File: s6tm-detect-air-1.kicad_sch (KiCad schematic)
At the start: 0 parts

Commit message: schem: import stm32f104 mcu
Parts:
- added C12: 10u, Capacitor_SMD:C_0805_2012Metric, symbol Device:C
- added C13, C16, C17, C18, C19: 0u1, Capacitor_SMD:C_0402_1005Metric, symbol Device:C
- added C14, C15: 20p, Capacitor_SMD:C_0603_1608Metric, symbol Device:C
- added C20, C21: 1u, Capacitor_SMD:C_0402_1005Metric, symbol Device:C
- added D10: YELLOW, LED_SMD:LED_0805_2012Metric, symbol Device:LED
- added D5, D6, D7, D8, D9: H5VU10U, GLCS:Diode_DFN1006, symbol GLCS:H5VU10U
- added FB1: 600Ω@100M, Inductor_SMD:L_0805_2012Metric, symbol Device:FerriteBead
- added J4: TC2030, Connector:Tag-Connect_TC2030-IDC-NL_2x03_P1.27mm_Vertical, symbol Connector:Conn_ARM_SWD_TagConnect_TC2030-NL
- added J5: Conn_01x04_Pin, Connector_PinHeader_2.54mm:PinHeader_1x04_P2.54mm_Vertical, symbol Connector:Conn_01x04_Pin
- added R10, R11, R9: 10k, Resistor_SMD:R_0402_1005Metric, symbol Device:R
- added R12: 560, Resistor_SMD:R_0603_1608Metric, symbol Device:R_Small
- added R13: 5k1, Resistor_SMD:R_0402_1005Metric, symbol Device:R
- added U6: STM32F103C8Tx, Package_QFP:LQFP-48_7x7mm_P0.5mm, symbol MCU_ST_STM32F1:STM32F103C8Tx
- added Y1: 8M, Crystal:Crystal_SMD_5032-2Pin_5.0x3.2mm, symbol Device:Crystal
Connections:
- new net: R13.1, U6.25 (PB12)
- new net: D10.2 (A), R13.2
- new net: C20.1, FB1.1, U6.9 (VDDA)
- new net +3V3: C12.1, C16.1, C17.1, C18.1, C19.1, C21.1, D9.1 (K), FB1.2, J4.1 (VCC), J5.1 (Pin_1), R10.1, R11.1, U6.1 (VBAT), U6.24 (VDD), U6.36 (VDD), U6.48 (VDD)
- new net BOOT: R9.2, U6.44 (BOOT0)
- new net CAN_RX: U6.45 (PB8)
- new net CAN_TX: U6.46 (PB9)
- new net GND: C12.2, C13.2, C14.2, C15.2, C16.2, C17.2, C18.2, C19.2, C20.2, C21.2, D10.1 (K), D5.2 (A), D6.2 (A), D7.2 (A), D8.2 (A), D9.2 (A), J4.5 (GND), J5.3 (Pin_3), R9.1, U6.20 (PB2), U6.23 (VSS), U6.35 (VSS), U6.47 (VSS), U6.8 (VSSA)
- new net NRST: C13.1, D8.1 (K), J4.3 (~{RESET}), U6.7 (NRST)
- new net SCL: R11.2
- new net SDA: R10.2
- new net SWCLK: D7.1 (K), J4.4 (SWCLK), U6.37 (PA14)
- new net SWDIO: D6.1 (K), J4.2 (SWDIO), U6.34 (PA13)
- new net SWO: D5.1 (K), J4.6 (SWO), U6.39 (PB3)
- new net U0RXD: J5.2 (Pin_2), U6.13 (PA3)
- new net U0TXD: J5.4 (Pin_4), U6.12 (PA2)
- new net XTAL_I: C14.1, U6.5 (PD0), Y1.2
- new net XTAL_O: R12.2, U6.6 (PD1)
- new net XTAL_RO: C15.1, R12.1, Y1.1
- no-connect marks 0 -> 5
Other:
- note added: "CAN Alive"
- note added: "Debug port"
- note added: "HSE"
- note added: "UART"

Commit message: schem: import HT753-1 3V3 LDO
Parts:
- added C1, C4: 10u, Capacitor_SMD:C_0805_2012Metric, symbol Device:C
- added TP2: TestPoint, TestPoint:TestPoint_Pad_D2.0mm, symbol Connector:TestPoint
- added U1: HT753-1, Package_TO_SOT_SMD:SOT-89-3, symbol Regulator_Linear:HT75xx-1-SOT89
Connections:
- net +3V3: now also C4.1, TP2.1, U1.3 (VOUT)
- net GND: now also C1.2, C4.2, U1.1 (GND)
- new net +5V: C1.1, U1.2 (VIN)
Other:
- note added: "HT753-1 3V3 LDO"

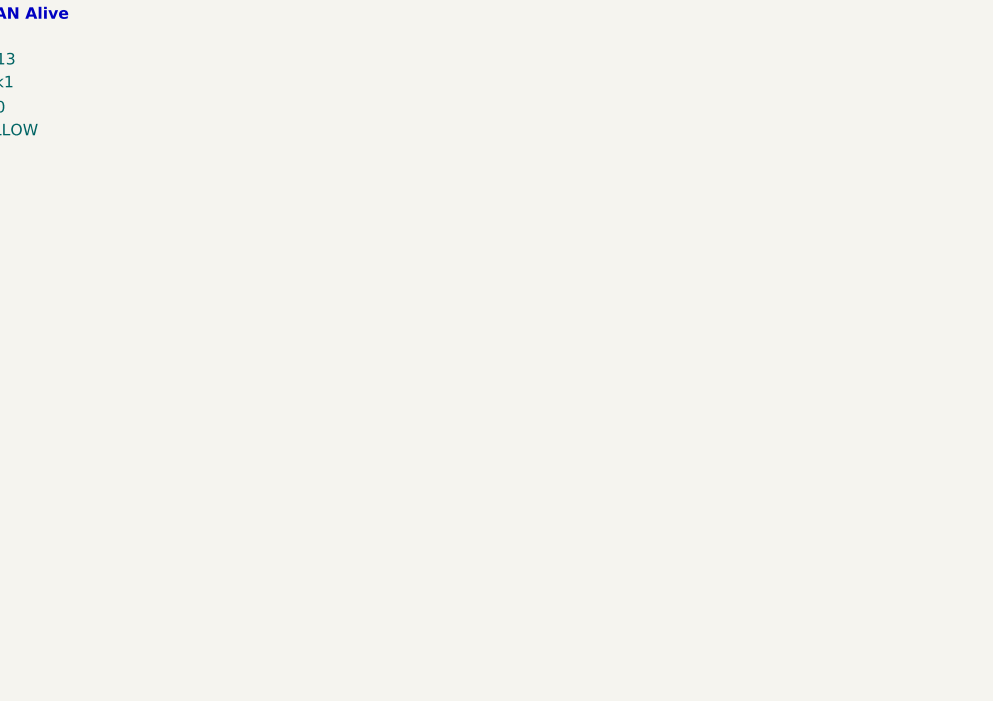
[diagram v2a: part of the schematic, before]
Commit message: schem: add LM73100 5V Input protection
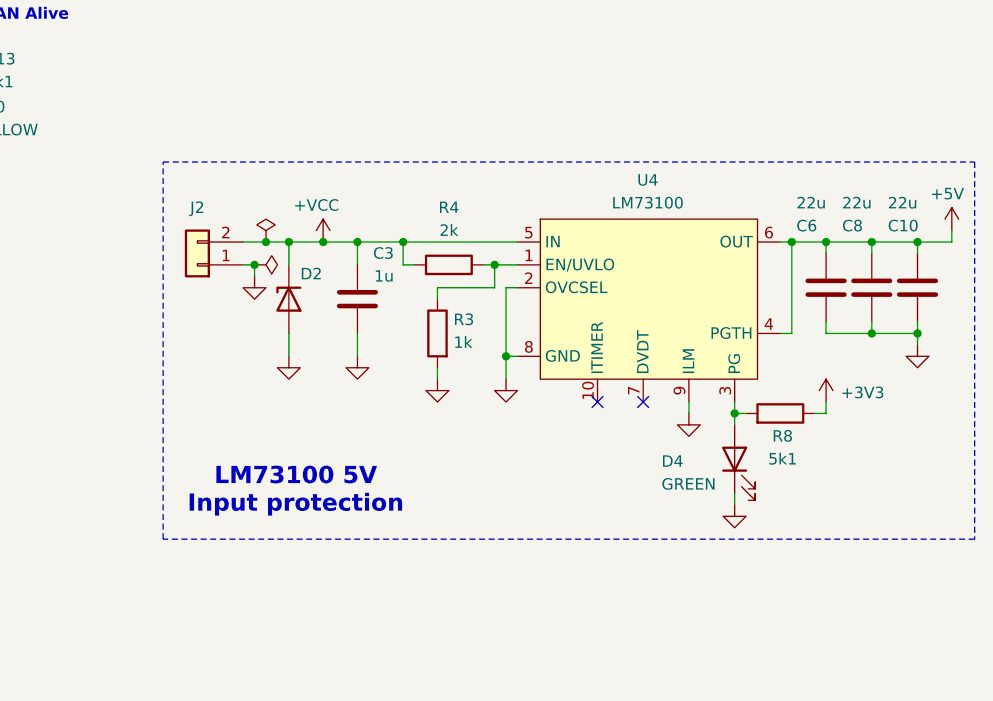
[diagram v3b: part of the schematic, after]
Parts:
- added C10, C6, C8: 22u, Capacitor_SMD:C_0805_2012Metric, symbol Device:C
- added C3: 1u, Capacitor_SMD:C_0402_1005Metric, symbol Device:C
- added D2: SMAJ12A, Diode_SMD:D_SMA, symbol Pers:H5VU10U
- added D4: GREEN, LED_SMD:LED_0805_2012Metric, symbol Device:LED
- added J2: Conn_01x02, TerminalBlock_Phoenix:TerminalBlock_Phoenix_MKDS-1,5-2-5.08_1x02_P5.08mm_Horizontal, symbol Connector_Generic:Conn_01x02
- added R3: 1k, Resistor_SMD:R_0402_1005Metric, symbol Device:R
- added R4: 2k, Resistor_SMD:R_0402_1005Metric, symbol Device:R
- added R8: 5k1, Resistor_SMD:R_0402_1005Metric, symbol Device:R
- added U4: LM73100, GLCS:Texas_RPW0010A_VQFN-HR-10_2x2mm_P0.5mm, symbol GLCS:LM73100
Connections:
- net +3V3: now also R8.1
- net +5V: now also C10.2, C6.2, C8.2, U4.4 (PGTH), U4.6 (OUT)
- net GND: now also C10.1, C3.1, C6.1, C8.1, D2.2 (A), D4.1 (K), J2.1 (Pin_1), R3.2, U4.2 (OVCSEL), U4.8 (GND), U4.9 (ILM)
- new net: D4.2 (A), R8.2, U4.3 (PG)
- new net: R3.1, R4.1, U4.1 (EN/UVLO)
- new net +VCC: C3.2, D2.1 (K), J2.2 (Pin_2), R4.2, U4.5 (IN)
- no-connect marks 5 -> 7
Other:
- note added: "LM73100 5V Input protection"

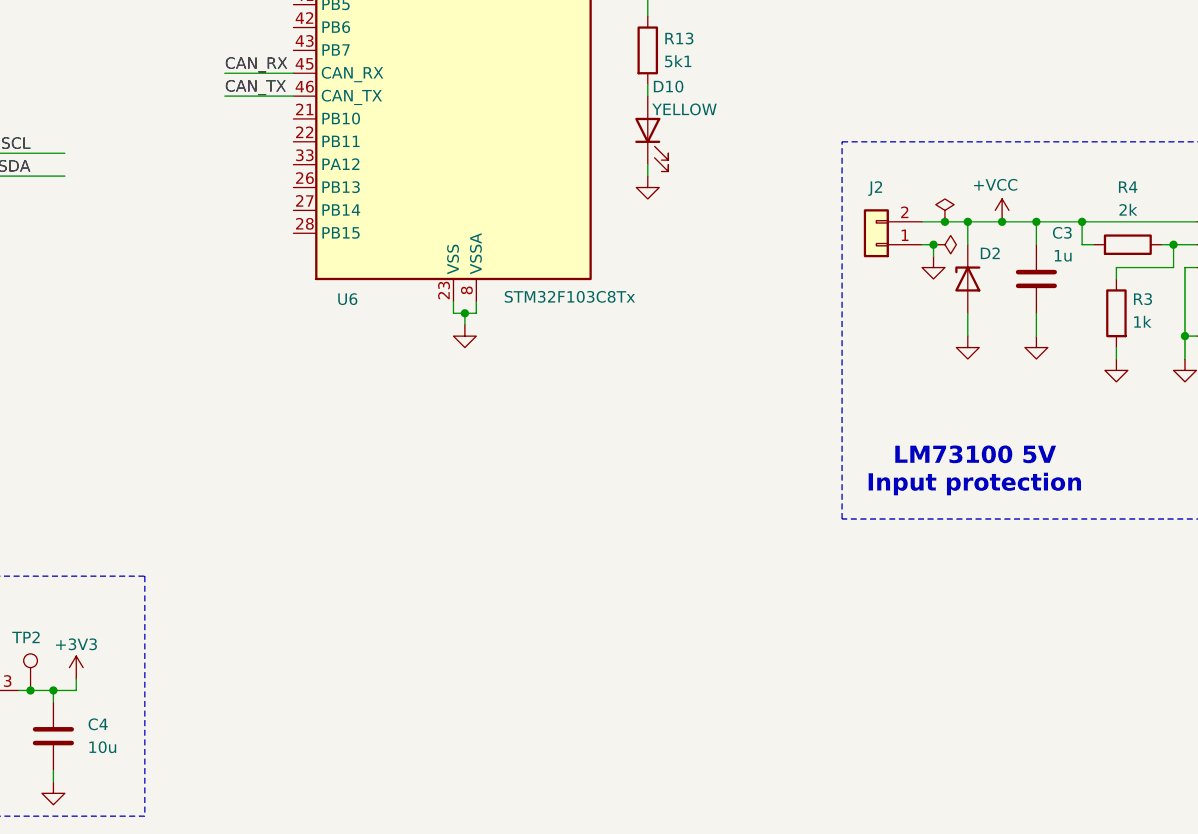
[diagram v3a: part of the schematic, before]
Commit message: schem: import can transceiver and connector
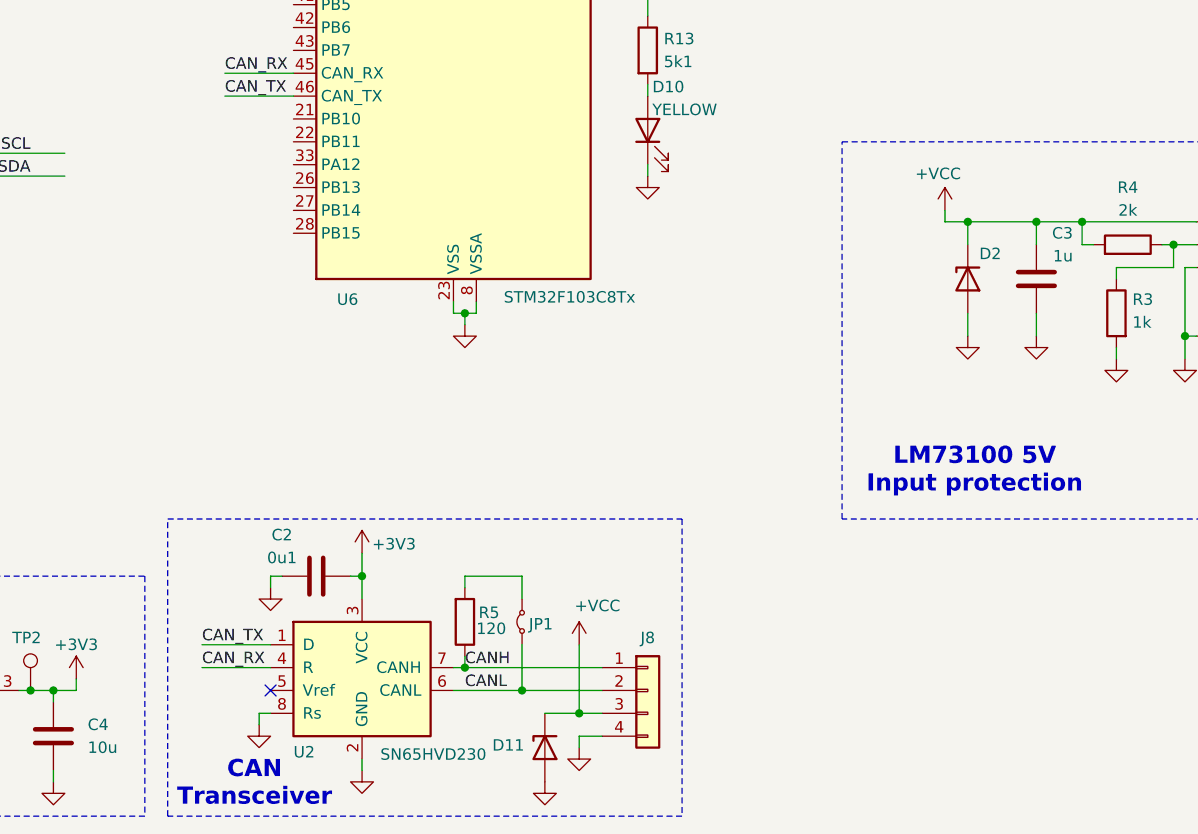
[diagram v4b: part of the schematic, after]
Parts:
- removed J2: Conn_01x02, TerminalBlock_Phoenix:TerminalBlock_Phoenix_MKDS-1,5-2-5.08_1x02_P5.08mm_Horizontal, symbol Connector_Generic:Conn_01x02
- added C2: 0u1, Capacitor_SMD:C_0402_1005Metric, symbol Device:C
- added D11: H5VU10U, GLCS:Diode_DFN1006, symbol GLCS:H5VU10U
- added J8: Conn_01x04, Connector_JST:JST_XH_S4B-XH-A-1_1x04_P2.50mm_Horizontal, symbol Connector_Generic:Conn_01x04
- added JP1: Jumper_2_Small_Bridged, Jumper:SolderJumper-2_P1.3mm_Open_RoundedPad1.0x1.5mm, symbol Jumper:Jumper_2_Small_Bridged
- added R5: 120, Resistor_SMD:R_1206_3216Metric, symbol Device:R
- added U2: SN65HVD230, Package_SO:SOIC-8_3.9x4.9mm_P1.27mm, symbol Interface_CAN_LIN:SN65HVD230
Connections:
- net +3V3: now also C2.1, U2.3 (VCC)
- net +VCC: now also D11.1 (K), J8.3 (Pin_3)
- net CAN_RX: now also U2.4 (R)
- net CAN_TX: now also U2.1 (D)
- net GND: now also C2.2, D11.2 (A), J8.4 (Pin_4), U2.2 (GND), U2.8 (Rs)
- new net: JP1.2 (B), R5.2
- new net CANH: J8.1 (Pin_1), R5.1, U2.7 (CANH)
- new net CANL: J8.2 (Pin_2), JP1.1 (A), U2.6 (CANL)
- no-connect marks 7 -> 8
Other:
- note added: "CAN Transceiver"

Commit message: schem: add boot/rst buttons
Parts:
- added SW1, SW5: SW_Push, Button_Switch_SMD:SW_SPST_TS-1088-xR020, symbol Switch:SW_Push
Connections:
- net +3V3: now also SW1.1
- net BOOT: now also SW1.2
- net GND: now also SW5.1
- net NRST: now also SW5.2
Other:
- note added: "Buttons"

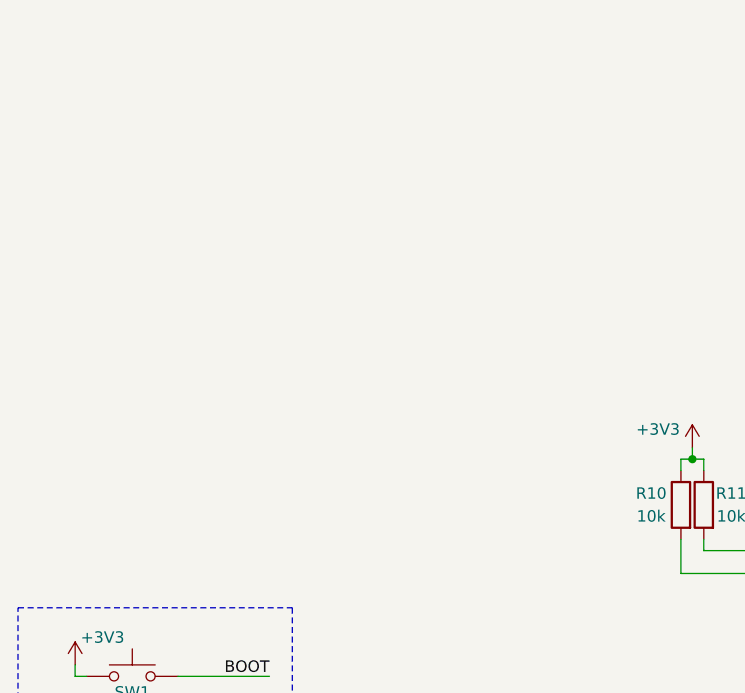
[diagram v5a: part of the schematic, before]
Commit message: schem: add MiCS-5524 MOS 1 Sensor
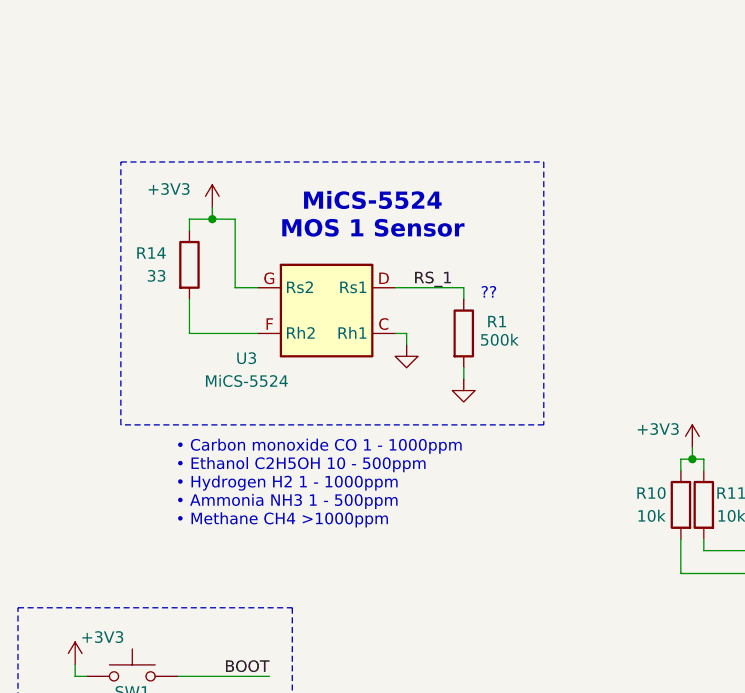
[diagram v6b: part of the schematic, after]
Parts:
- added R1: 500k, symbol Device:R
- added R14: 33, Resistor_SMD:R_0603_1608Metric, symbol Device:R
- added U3: MiCS-5524, Sensor:Sensortech_MiCS_5x7mm_P1.25mm, symbol Sensor_Gas:MiCS-5524
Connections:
- net +3V3: now also R14.1, U3.G (Rs2)
- net GND: now also R1.2, U3.C (Rh1)
- new net: R14.2, U3.F (Rh2)
- new net RS_1: R1.1, U3.D (Rs1)
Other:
- note added: "??"
- note added: "MiCS-5524 MOS 1 Sensor"
- note added: "• Carbon monoxide CO 1 - 1000ppm • Ethanol C2H5OH 10 - 500ppm • Hydrogen H2 1 - 1000ppm • Ammonia NH3 1 - 500ppm • Methane CH4 >1000ppm"

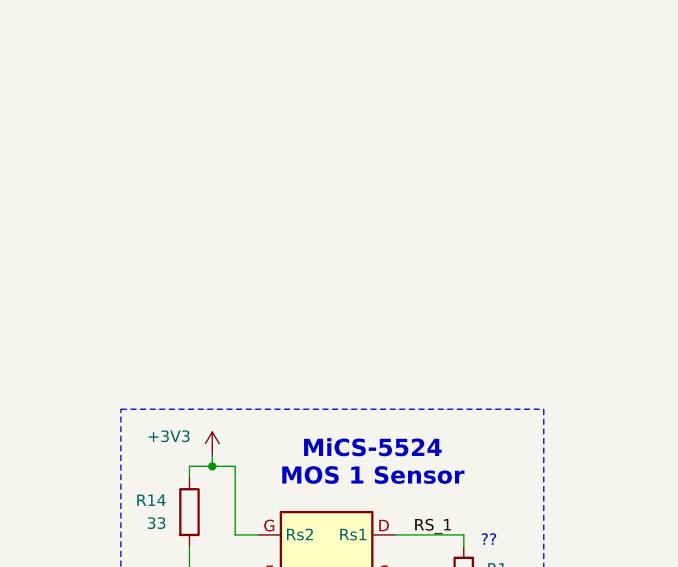
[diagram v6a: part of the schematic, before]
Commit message: schem: add SGP41 module connector
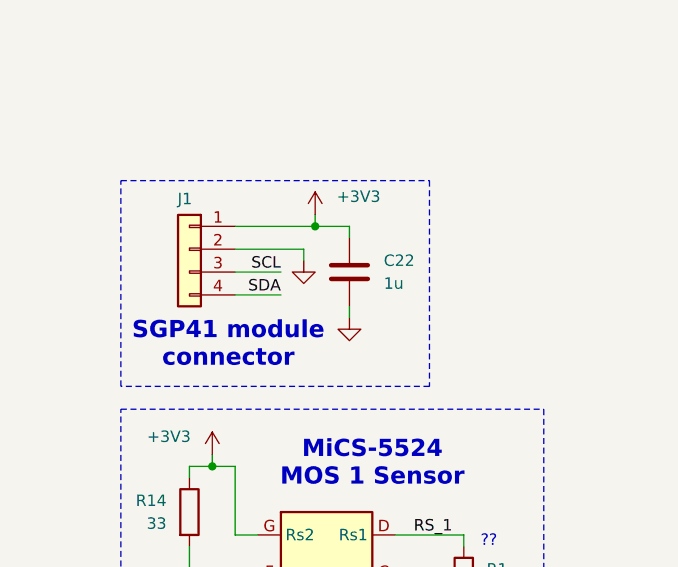
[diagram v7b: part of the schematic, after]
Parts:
- added C22: 1u, Capacitor_SMD:C_0402_1005Metric, symbol Device:C
- added J1: Conn_01x04, symbol Connector_Generic:Conn_01x04
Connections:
- net +3V3: now also C22.2, J1.1 (Pin_1)
- net GND: now also C22.1, J1.2 (Pin_2)
- net SCL: now also J1.3 (Pin_3)
- net SDA: now also J1.4 (Pin_4)
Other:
- note added: "SGP41 module connector"

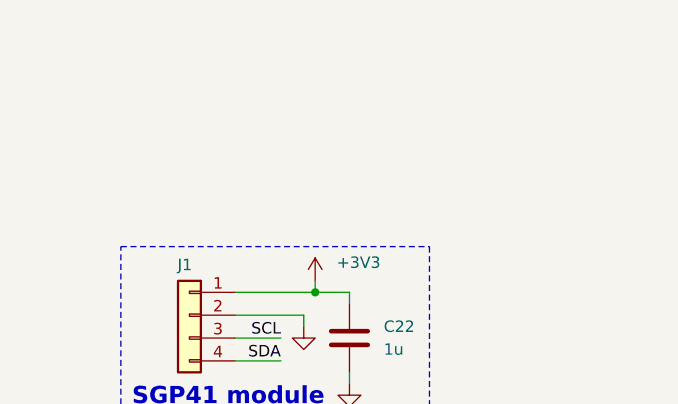
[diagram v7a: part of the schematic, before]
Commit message: schem: add SCD41 module connector
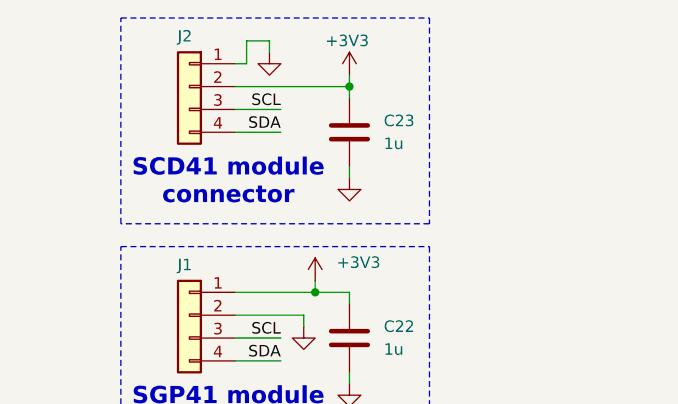
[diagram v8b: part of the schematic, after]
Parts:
- added C23: 1u, Capacitor_SMD:C_0402_1005Metric, symbol Device:C
- added J2: Conn_01x04, symbol Connector_Generic:Conn_01x04
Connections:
- net +3V3: now also C23.2, J2.2 (Pin_2)
- net GND: now also C23.1, J2.1 (Pin_1)
- net SCL: now also J2.3 (Pin_3)
- net SDA: now also J2.4 (Pin_4)
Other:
- note added: "SCD41 module connector"
